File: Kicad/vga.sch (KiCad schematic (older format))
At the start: 1 part, among them J14 DB15_Female_HighDensity_Mount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

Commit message: Adding VGA output buffer/filter.
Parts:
- added C701: 4.7u, symbol Device:C
- added C702: 100n, symbol Device:C
- added R701, R702, R703, R704, R705, R706, R710, R711, R712, R716, R717, R718, R722, R723, R724, R728, R729, R730, R732: 24K, symbol Device:R
- added R707, R708, R709, R713, R714, R715, R719, R720, R721, R725, R726, R727, R731: 12K, symbol Device:R
- added R733, R734, R735: 3K3, symbol Device:R
- added R736, R737, R738: 75, symbol Device:R
- added R739: 0, symbol Device:R
- added R740, R741: 470, symbol Device:R
- added U701: TPF133A, Package_SO:SOIC-8_3.9x4.9mm_P1.27mm, symbol NeotronF7:TPF133A
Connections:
- net labels added: +3.3V, ANALOG_BLUE, ANALOG_GREEN, ANALOG_RED, BOUT, B[0], B[1], B[2], B[3], B[4], GND, GOUT, G[0], G[1], G[2], G[3], G[4], G[5], HSYNC, RED0, RED1, RED2, RED3, RED4, RED[0..4], ROUT, VSYNC
- wire segments 0 -> 116
- no-connect marks 0 -> 6
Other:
- note added: "0.7V peak input\n6dB Gain\n1.4V peak output"
- note added: "5-bit R2R DAC\n3.3V * 31 / 32 = 3.196875 V\nBuffer Input = 3.196875 V * 3300 / (12000 + 3300) = 690mV\n"
- note added: "6-bit R2R DAC\n3.3V * 63 / 64 = 3.2484375 V\nBuffer Input = 3.2484375 V * 3300 / (12000 + 3300) = 701mV\n"
- note added: "75R output impedance here\nand 75R input impedance in monitor\ngives 0.7V peak inside monitor"
- note added: "LSB"
- note added: "MSB"
- note added: "Place near IC"
- note added: "Video Filter / Buffer"
- moved on the sheet: J14

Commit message: Renamed to Neotron-528ST
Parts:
- U701: symbol NeotronF7:TPF133A -> Neotron-528ST:TPF133A
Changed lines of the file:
@@
 $EndComp
 $Comp
-L NeotronF7:TPF133A U701
+L Neotron-528ST:TPF133A U701
 U 1 1 5EE35D56
 P 7100 3250

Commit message: Removed USB FS hub. Added stacked USB A connector.
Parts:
- C701: footprint (none) -> Capacitor_SMD:C_0805_2012Metric
- C702: footprint (none) -> Capacitor_SMD:C_0402_1005Metric
- J701: renamed from J14; footprint (none) -> Connector_Dsub:DSUB-15-HD_Female_Horizontal_P2.29x1.98mm_EdgePinOffset3.03mm_Housed_MountingHolesOffset4.94mm
- R701: renamed from R703; footprint (none) -> Resistor_SMD:R_0402_1005Metric
- R702: renamed from R711; footprint (none) -> Resistor_SMD:R_0402_1005Metric
- R703: renamed from R717; footprint (none) -> Resistor_SMD:R_0402_1005Metric
- R704: renamed from R723; footprint (none) -> Resistor_SMD:R_0402_1005Metric
- R705: renamed from R729; footprint (none) -> Resistor_SMD:R_0402_1005Metric
- R706: renamed from R708; footprint (none) -> Resistor_SMD:R_0402_1005Metric
- R707: renamed from R714; footprint (none) -> Resistor_SMD:R_0402_1005Metric
- R708: renamed from R720; footprint (none) -> Resistor_SMD:R_0402_1005Metric
- R709: renamed from R726; footprint (none) -> Resistor_SMD:R_0402_1005Metric
- R710: renamed from R733; footprint (none) -> Resistor_SMD:R_0402_1005Metric
- R711: renamed from R704; footprint (none) -> Resistor_SMD:R_0402_1005Metric
- R712: renamed from R736; footprint (none) -> Resistor_SMD:R_0402_1005Metric
- R713: renamed from R737; footprint (none) -> Resistor_SMD:R_0402_1005Metric
- R714: renamed from R738; footprint (none) -> Resistor_SMD:R_0402_1005Metric
- R715: renamed from R740; footprint (none) -> Resistor_SMD:R_0402_1005Metric
- R716: renamed from R741; footprint (none) -> Resistor_SMD:R_0402_1005Metric
- R717: renamed from R705; footprint (none) -> Resistor_SMD:R_0402_1005Metric
- R718: renamed from R712; footprint (none) -> Resistor_SMD:R_0402_1005Metric
- R719: renamed from R718; footprint (none) -> Resistor_SMD:R_0402_1005Metric
- R720: renamed from R724; footprint (none) -> Resistor_SMD:R_0402_1005Metric
- R721: renamed from R730; footprint (none) -> Resistor_SMD:R_0402_1005Metric
- R722: renamed from R732; footprint (none) -> Resistor_SMD:R_0402_1005Metric
- R723: renamed from R739; footprint (none) -> Resistor_SMD:R_0402_1005Metric
- R724: renamed from R709; footprint (none) -> Resistor_SMD:R_0402_1005Metric
- R725: renamed from R715; footprint (none) -> Resistor_SMD:R_0402_1005Metric
- R726: renamed from R721; footprint (none) -> Resistor_SMD:R_0402_1005Metric
- R727: footprint (none) -> Resistor_SMD:R_0402_1005Metric
- R728: renamed from R731; footprint (none) -> Resistor_SMD:R_0402_1005Metric
- R729: renamed from R706; footprint (none) -> Resistor_SMD:R_0402_1005Metric
- R730: renamed from R734; footprint (none) -> Resistor_SMD:R_0402_1005Metric
- R731: renamed from R701; footprint (none) -> Resistor_SMD:R_0402_1005Metric
- R732: renamed from R710; footprint (none) -> Resistor_SMD:R_0402_1005Metric
- R733: renamed from R716; footprint (none) -> Resistor_SMD:R_0402_1005Metric
- R734: renamed from R722; footprint (none) -> Resistor_SMD:R_0402_1005Metric
- R735: renamed from R728; footprint (none) -> Resistor_SMD:R_0402_1005Metric
- R736: renamed from R707; footprint (none) -> Resistor_SMD:R_0402_1005Metric
- R737: renamed from R713; footprint (none) -> Resistor_SMD:R_0402_1005Metric
- R738: renamed from R719; footprint (none) -> Resistor_SMD:R_0402_1005Metric
- R739: renamed from R725; footprint (none) -> Resistor_SMD:R_0402_1005Metric
- R740: renamed from R702; footprint (none) -> Resistor_SMD:R_0402_1005Metric
- R741: renamed from R735; footprint (none) -> Resistor_SMD:R_0402_1005Metric
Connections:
- net labels added: BLUE3, BLUE4, BLUE5, BLUE6, BLUE7, BLUE[7..3], GREEN2, GREEN3, GREEN4, GREEN5, GREEN6, GREEN7, GREEN[7..2], RED5, RED6, RED7, RED[7..3]
- net labels removed: B[0], B[1], B[2], B[3], B[4], G[0], G[1], G[2], G[3], G[4], G[5], RED0, RED1, RED2, RED[0..4]
- wire segments 116 -> 110
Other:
- note added: "Place near U701"
- note added: "TBD: Should we support DDC2?\nPin 9: +5V\nPin 12: SDA\nPin 15: SCL"
- note removed: "Place near IC"
- moved on the sheet: R701, R702, R703, R704, R705, R706, R707, R708, R709, R711, R717, R718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

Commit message: Swap to H7 in the Schematic
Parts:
- U701: symbol Neotron-528ST:TPF133A -> Neotron-500:TPF133A
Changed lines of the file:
@@
 $EndComp
 $Comp
-L Neotron-528ST:TPF133A U701
+L Neotron-500:TPF133A U701
 U 1 1 5EE35D56
 P 7100 3150

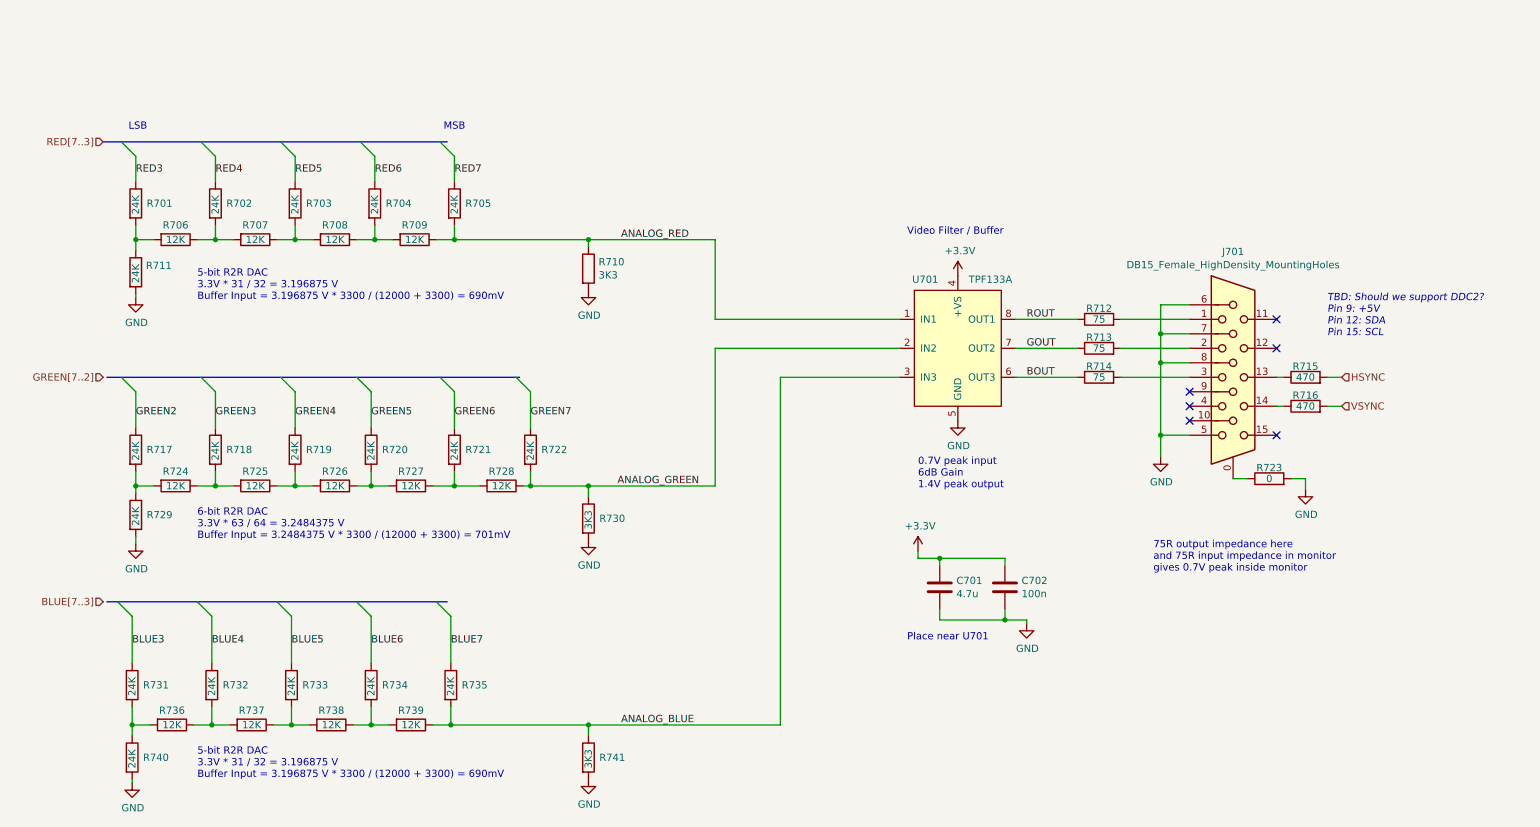
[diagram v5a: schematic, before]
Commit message: Tidying up schematic, and README.
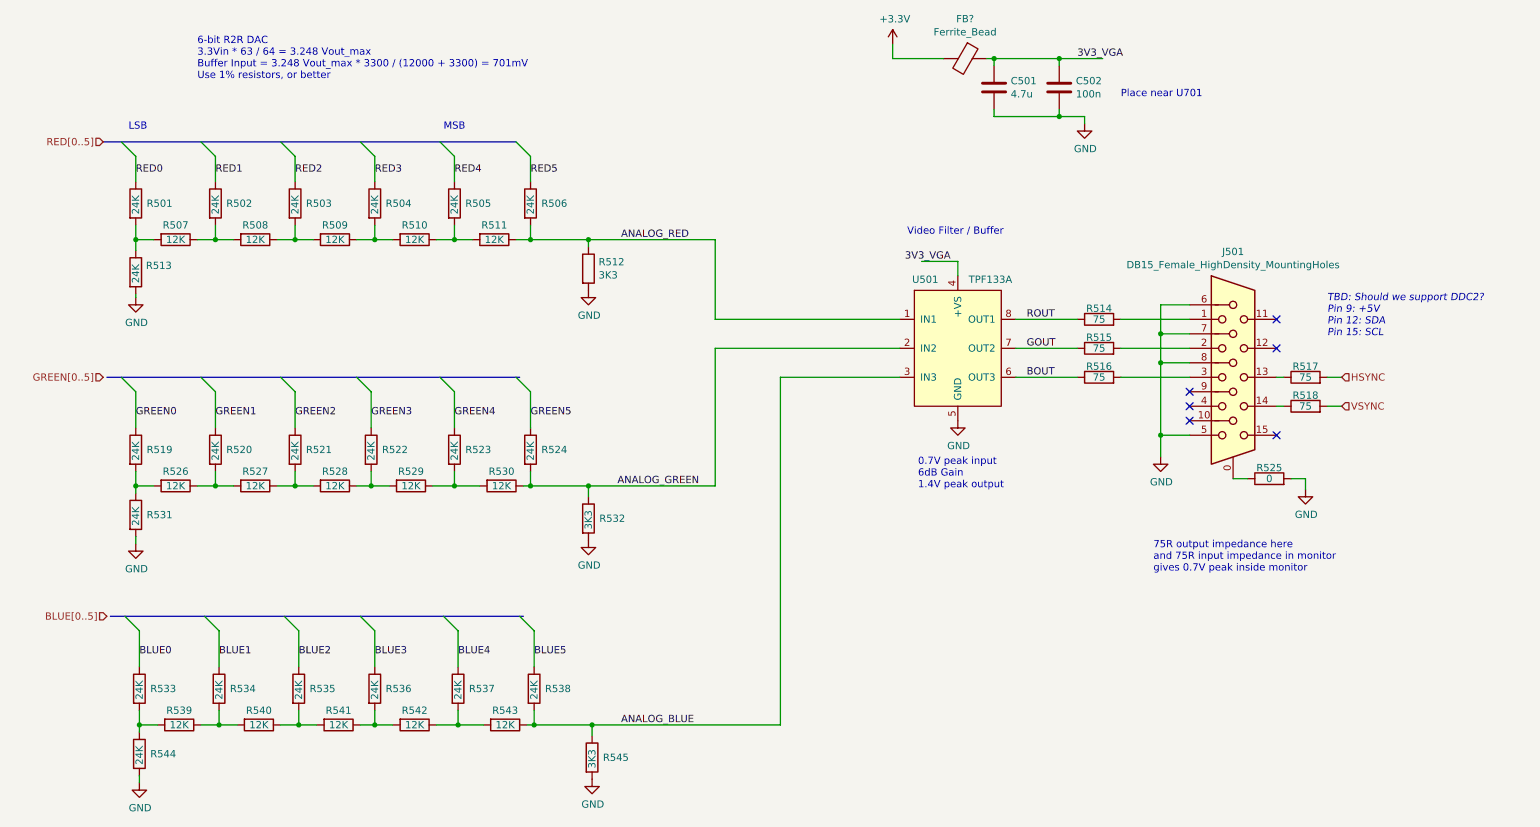
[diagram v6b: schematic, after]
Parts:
- removed R731, R732, R733, R734, R735, R740: 24K, Resistor_SMD:R_0402_1005Metric, symbol Device:R
- removed R736, R737, R738, R739: 12K, Resistor_SMD:R_0402_1005Metric, symbol Device:R
- removed R741: 3K3, Resistor_SMD:R_0402_1005Metric, symbol Device:R
- added FB?: Ferrite_Bead, symbol Device:Ferrite_Bead
- added R506, R533, R534, R535, R536, R537, R538, R544: 24K, Resistor_SMD:R_0402_1005Metric, symbol Device:R
- added R511, R539, R540, R541, R542, R543: 12K, Resistor_SMD:R_0402_1005Metric, symbol Device:R
- added R545: 3K3, Resistor_SMD:R_0402_1005Metric, symbol Device:R
- R517: renamed from R715; value 470 -> 75
- R518: renamed from R716; value 470 -> 75
- renumbered C701 to C501, C702 to C502, J701 to J501, R701 to R501, R702 to R502, R703 to R503, R704 to R504, R705 to R505, R706 to R507, R707 to R508, R708 to R509, R709 to R510, R710 to R512, R711 to R513, R712 to R514, R713 to R515, R714 to R516, R717 to R519, R718 to R520, R719 to R521, R720 to R522, R721 to R523, R722 to R524, R723 to R525, R724 to R526, R725 to R527, R726 to R528, R727 to R529, R728 to R530, R729 to R531, R730 to R532, U701 to U501
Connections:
- net GREEN6 is gone; now on net GREEN4: R523.1
- net GREEN7 is gone; now on net GREEN5: R524.1
- net RED6 is gone; now on net RED3: R504.1
- net RED7 is gone; now on net RED4: R505.1
- net +3V3: now also FB?.2; no longer C501.1, C502.1, U501.4 (+VS)
- net ANALOG_BLUE: now also R538.2, R543.1, R545.1
- net ANALOG_RED: now also R506.2, R511.1; no longer R505.2, R510.1
- net BLUE3: now also R536.1
- net BLUE4: now also R537.1
- net BLUE5: now also R538.1
- net GND: now also R544.2, R545.2
- net GREEN2: now also R521.1; no longer R519.1
- net GREEN3: now also R522.1; no longer R520.1
- net GREEN4: no longer R521.1
- net GREEN5: no longer R522.1
- net RED3: no longer R501.1
- net RED4: no longer R502.1
- net RED5: now also R506.1; no longer R503.1
- new net: R505.2, R510.1, R511.2
- new net: R533.2, R539.2, R544.1
- new net: R534.2, R539.1, R540.2
- new net: R535.2, R540.1, R541.2
- new net: R536.2, R541.1, R542.2
- new net: R537.2, R542.1, R543.2
- new net 3V3_VGA: C501.1, C502.1, FB?.1, U501.4 (+VS)
- new net BLUE0: R533.1
- new net BLUE1: R534.1
- new net BLUE2: R535.1
- new net GREEN0: R519.1
- new net GREEN1: R520.1
- new net RED0: R501.1
- new net RED1: R502.1
- new net RED2: R503.1
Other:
- note added: "6-bit R2R DAC\n3.3Vin * 63 / 64 = 3.248 Vout_max\nBuffer Input = 3.248 Vout_max * 3300 / (12000 + 3300) = 701mV\nUse 1% resistors, or better"
- note removed: "5-bit R2R DAC\n3.3V * 31 / 32 = 3.196875 V\nBuffer Input = 3.196875 V * 3300 / (12000 + 3300) = 690mV\n"
- note removed: "6-bit R2R DAC\n3.3V * 63 / 64 = 3.2484375 V\nBuffer Input = 3.2484375 V * 3300 / (12000 + 3300) = 701mV\n"
- moved on the sheet: C501, C502
